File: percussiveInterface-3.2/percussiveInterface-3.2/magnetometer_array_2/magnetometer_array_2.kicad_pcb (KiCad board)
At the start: 4 copper layers, 180 x 25.4 mm, 69 parts, among them J1 Conn_01x05_Socket, J2 Conn_01x08_Socket, J3 Conn_01x08_Socket, J4 Conn_01x08_Socket, J5 Conn_01x08_Socket, U1 SM225-10E, U10 SM225-10E, U11 SM225-10E, U12 SM225-10E, U13 SM225-10E, U14 SM225-10E, U15 SM225-10E, U16 SM225-10E, U17 SM225-10E, U18 SM225-10E, U19 SM225-10E, U2 SM225-10E, U20 SM225-10E, U21 SM225-10E, U22 SM225-10E, U23 SM225-10E, U24 SM225-10E, U25 SM225-10E, U26 SM225-10E, U27 SM225-10E, U28 SM225-10E, U29 SM225-10E, U3 SM225-10E, U30 SM225-10E, U31 SM225-10E, U32 SM225-10E, U4 SM225-10E, U5 SM225-10E, U6 SM225-10E, U7 SM225-10E, U8 SM225-10E, U9 SM225-10E

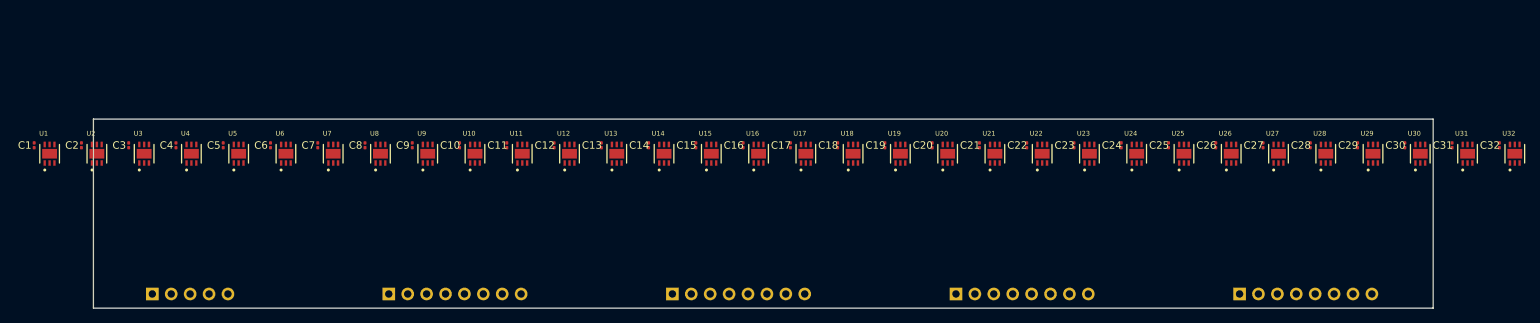
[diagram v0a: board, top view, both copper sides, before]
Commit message: new magnetoarray
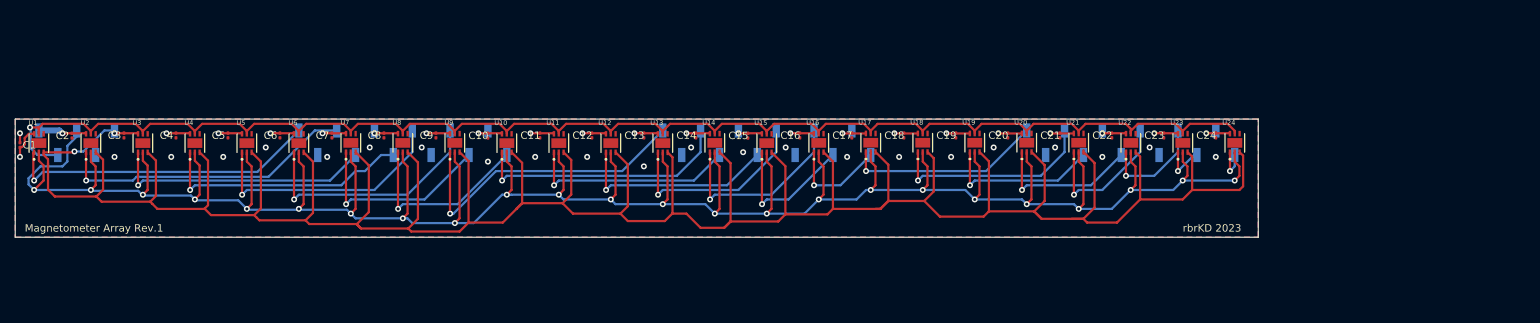
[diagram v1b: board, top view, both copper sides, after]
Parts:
- removed C25, C26, C27, C28, C29, C30, C31, C32: C_Small, Capacitor_SMD:C_0201_0603Metric
- removed J5: Conn_01x08_Socket, Connector_PinSocket_2.54mm:PinSocket_1x08_P2.54mm_Horizontal
- removed U25, U26, U27, U28, U29, U30, U31, U32: SM225-10E, NVE:SON65P250X250X80-7N
- J1: footprint Connector_PinSocket_2.54mm:PinSocket_1x05_P2.54mm_Horizontal -> Connector_PinSocket_2.54mm:PinSocket_1x05_P2.54mm_Vertical_SMD_Pin1Left
- J2, J3, J4: value Conn_01x08_Socket -> Conn_01x12_Socket; footprint Connector_PinSocket_2.54mm:PinSocket_1x08_P2.54mm_Horizontal -> Connector_PinSocket_2.54mm:PinSocket_1x12_P2.54mm_Vertical_SMD_Pin1Left
- moved J4 31.0 mm to (188.0, 66.7)
- moved J3 24.0 mm to (139.1, 66.7)
- moved J1 22.7 mm to (46.4, 66.7)
- moved J2 20.4 mm to (90.2, 66.7)
- moved U24 13.3 mm to (201.9, 66.7)
- moved C24 12.8 mm to (199.4, 65.7)
- moved U23 12.6 mm to (195.0, 66.7)
- moved C23 12.1 mm to (192.4, 65.7)
- moved U22 12.0 mm to (188.0, 66.7)
- moved C22 11.5 mm to (185.4, 65.7)
- moved U21 11.4 mm to (181.0, 66.7)
- moved C21 10.9 mm to (178.4, 65.7)
- moved U20 10.7 mm to (174.0, 66.7)
- moved C20 10.2 mm to (171.4, 65.7)
- moved U19 10.1 mm to (167.0, 66.7)
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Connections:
- U10 pad 1: SS1 -> SS10
- U11 pad 1: SS1 -> SS11
- U12 pad 1: SS1 -> SS12
- U13 pad 1: SS1 -> SS13
- U14 pad 1: SS1 -> SS14
- U15 pad 1: SS1 -> SS15
- U16 pad 1: SS1 -> SS16
- U17 pad 1: SS1 -> SS17
- U18 pad 1: SS1 -> SS18
- U19 pad 1: SS1 -> SS19
- U2 pad 1: SS1 -> SS2
- U20 pad 1: SS1 -> SS20
- U21 pad 1: SS1 -> SS21
- U22 pad 1: SS1 -> SS22
- U23 pad 1: SS1 -> SS23
- U24 pad 1: SS1 -> SS24
- U3 pad 1: SS1 -> SS3
- U4 pad 1: SS1 -> SS4
- U5 pad 1: SS1 -> SS5
- U6 pad 1: SS1 -> SS6
- U7 pad 1: SS1 -> SS7
- U8 pad 1: SS1 -> SS8
- U9 pad 1: SS1 -> SS9
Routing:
- net MISO: track 0.00 -> 390.4 mm, vias 0 -> 1
- net MOSI: track 0.00 -> 350.9 mm, vias 0 -> 24
- net SCLK: track 0.00 -> 197.4 mm, vias 0 -> 1
- net v+: track 0.00 -> 81.0 mm, vias 0 -> 24
- net SS1: track 0.00 -> 42.2 mm, vias 0 -> 1
- net SS9: track 0.00 -> 41.5 mm, vias 0 -> 1
- net SS2: track 0.00 -> 40.2 mm, vias 0 -> 1
- net SS3: track 0.00 -> 35.3 mm, vias 0 -> 1
- net SS10: track 0.00 -> 35.0 mm, vias 0 -> 1
- net SS4: track 0.00 -> 34.3 mm, vias 0 -> 1
- net SS5: track 0.00 -> 33.8 mm, vias 0 -> 1
- net SS6: track 0.00 -> 32.8 mm, vias 0 -> 1
- net SS11: track 0.00 -> 28.3 mm, vias 0 -> 1
- net SS18: track 0.00 -> 28.0 mm, vias 0 -> 1
- net SS12: track 0.00 -> 27.3 mm, vias 0 -> 1
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- added copper zone on B.Cu, net GND
- added copper zone on F.Cu, net GND
- added copper zone on In1.Cu, net GND
- added copper zone on In2.Cu, net v+
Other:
- board size 180 x 25.4 mm -> 167 x 15.9 mm
- board text added: "Magnetometer Array Rev.1"
- board text added: "rbrKD 2023"

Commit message: new arrray
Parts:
- J1: footprint Connector_PinSocket_2.54mm:PinSocket_1x05_P2.54mm_Vertical_SMD_Pin1Left -> Connector_Harwin:Harwin_M20-89005xx_1x05_P2.54mm_Horizontal
- J2, J3, J4: footprint Connector_PinSocket_2.54mm:PinSocket_1x12_P2.54mm_Vertical_SMD_Pin1Left -> Connector_Harwin:Harwin_M20-89012xx_1x12_P2.54mm_Horizontal
- moved J2 15.0 mm to (78.1, 57.8), turned to 90 degrees
- moved U15 14.5 mm to (141.0, 52.4)
- moved U13 14.5 mm to (127.0, 52.4)
- moved U12 14.4 mm to (120.0, 52.4)
- moved U11 14.4 mm to (113.0, 52.4)
- moved U24 14.4 mm to (204.0, 52.4)
- moved U10 14.4 mm to (106.0, 52.4)
- moved U23 14.4 mm to (197.0, 52.4)
- moved U22 14.4 mm to (190.0, 52.4)
- moved U6 14.4 mm to (78.0, 52.4)
- moved U5 14.4 mm to (71.0, 52.4)
- moved U4 14.4 mm to (64.0, 52.4)
- moved U16 14.4 mm to (148.0, 52.4)
- moved U3 14.4 mm to (57.0, 52.4)
- moved U2 14.4 mm to (50.0, 52.4)
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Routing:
- net MOSI: track 350.9 -> 220.4 mm
- net MISO: track 390.4 -> 267.2 mm
- net SS6: track 32.8 -> 15.6 mm
- net SCLK: track 197.4 -> 214.2 mm
- net SS5: track 33.8 -> 17.5 mm
- net SS7: track 26.2 -> 11.2 mm
- net SS8: track 25.2 -> 10.4 mm
- net SS1: track 42.2 -> 27.7 mm
- net v+: track 81.0 -> 93.9 mm, vias 24 -> 25
- net SS9: track 41.5 -> 29.3 mm
- net SS4: track 34.3 -> 22.3 mm
- net SS2: track 40.2 -> 28.3 mm
- net SS3: track 35.3 -> 24.2 mm
- net SS14: track 25.9 -> 15.7 mm
- net SS13: track 26.9 -> 17.5 mm
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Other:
- board size 167 x 15.9 mm -> 167 x 16 mm
- board text added: "CLCK"
- board text added: "CS1"
- board text added: "CS10"
- board text added: "CS11"
- board text added: "CS12"
- board text added: "CS13"
- board text added: "CS14"
- board text added: "CS15"
- board text added: "CS16"
- board text added: "CS17"
- board text added: "CS18"
- board text added: "CS19"
- board text added: "CS2"
- board text added: "CS20"
- board text added: "CS21"
- board text added: "CS22"
- board text added: "CS23"
- board text added: "CS24"
- board text added: "CS3"
- board text added: "CS4"
- board text added: "CS5"
- board text added: "CS6"
- board text added: "CS7"
- board text added: "CS8"
- board text added: "CS9"
- board text added: "GND"
- board text added: "MISO"
- board text added: "MOSI"
- board text added: "SM225 MAGNETOMETER ARRAY"
- board text added: "V+"
- board text removed: "Magnetometer Array Rev.1"
